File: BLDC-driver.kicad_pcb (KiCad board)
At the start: 2 copper layers, 9 parts, among them Q1 IPD50R380CE, Q2 IPD50R380CE, Q3 IPD50R380CE, Q4 IPD50R380CE, U1 NCP81151

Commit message: Schematic progress
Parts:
- added C10: 100nF, Capacitor_SMD:C_0603_1608Metric, F.Cu at (155.2, 123.5)
- added C11: 4.7uF, Capacitor_SMD:C_0603_1608Metric, F.Cu at (155.2, 126.0)
- added C12: 4.7uF, Capacitor_SMD:C_0603_1608Metric, F.Cu at (159.3, 123.5)
- added C5: 4.7uF, Capacitor_SMD:C_0603_1608Metric, F.Cu at (159.3, 126.0)
- added C6: 100nF, Capacitor_SMD:C_0603_1608Metric, F.Cu at (147.2, 123.5)
- added C7: 4.7uF, Capacitor_SMD:C_0603_1608Metric, F.Cu at (151.2, 123.5)
- added C8: 4.7uF, Capacitor_SMD:C_0603_1608Metric, F.Cu at (147.2, 126.0)
- added C9: 4.7uF, Capacitor_SMD:C_0603_1608Metric, F.Cu at (151.2, 126.0)
- added Q5: FDMS86550, Package_TO_SOT_SMD:TDSON-8-1, B.Cu at (205.4, 108.4)
- added Q6: FDMS86550, Package_TO_SOT_SMD:TDSON-8-1, B.Cu at (204.3, 101.9)
- added U2: NCP81151, Package_DFN_QFN:DFN-8-1EP_2x2mm_P0.5mm_EP0.9x1.3mm, F.Cu at (207.3, 114.1)
- added U3: NCP81151, Package_DFN_QFN:DFN-8-1EP_2x2mm_P0.5mm_EP0.9x1.3mm, F.Cu at (189.8, 113.4)
- added U4: LPC1112FHN33-101, Package_DFN_QFN:QFN-32-1EP_7x7mm_P0.65mm_EP4.7x4.7mm, F.Cu at (177.3, 121.7)
- Q1, Q2, Q3, Q4: value IPD50R380CE -> FDMS86550; footprint Package_TO_SOT_SMD:TO-252-2 -> Package_TO_SOT_SMD:TDSON-8-1; moved to B.Cu
- moved C1 34.7 mm to (196.9, 111.7), turned to 180 degrees
- moved U1 30.4 mm to (196.9, 114.0)
- moved Q2 18.3 mm to (188.3, 101.9)
- moved Q4 16.5 mm to (196.6, 101.9), turned to 0 degrees
- moved Q1 13.1 mm to (189.4, 108.4), turned to 270 degrees
- moved Q3 9.89 mm to (197.5, 108.4), turned to 270 degrees
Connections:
- Q1 pad 1: Net-(Q1-Pad1) -> /PH_C
- Q1 pad 2: +24V -> /PH_C
- Q1 pad 3: /PH_A -> /PH_C
- Q2 pad 1: Net-(Q2-Pad1) -> GND
- Q2 pad 2: /PH_A -> GND
- Q3 pad 1: Net-(Q1-Pad1) -> /PH_A
- Q3 pad 2: +24V -> /PH_A
- Q4 pad 1: Net-(Q2-Pad1) -> GND
- Q4 pad 2: /PH_A -> GND
- U1 pad 2: Net-(U1-Pad2) -> (no net)
- U1 pad 3: Net-(U1-Pad3) -> (no net)
- U1 pad 5: Net-(Q2-Pad1) -> /LG_A
- U1 pad 8: Net-(Q1-Pad1) -> /HG_A
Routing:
- net GND: track 0.00 -> 7.62 mm
- net /PH_C: track 0.00 -> 5.61 mm, vias 0 -> 16
- net /PH_B: track 0.00 -> 4.89 mm, vias 0 -> 16
- net /PH_A: track 0.00 -> 4.89 mm, vias 0 -> 16
- net Net-(C1-Pad2): track 0.00 -> 1.64 mm
- added copper zone on B.Cu, net /PH_A
- added copper zone on B.Cu, net /PH_B
- added copper zone on B.Cu, net /PH_C
- added copper zone on F.Cu, net /PH_C
- added copper zone on B.Cu, net GND
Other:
- board outline added: 55.4 x 55.6 mm

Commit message: Latest
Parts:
- added C13: 2.7nF, Capacitor_SMD:C_0603_1608Metric, F.Cu at (200.0, 105.4)
- added C14: 2.7nF, Capacitor_SMD:C_0603_1608Metric, F.Cu at (208.0, 105.2)
- added C15: 2.7nF, Capacitor_SMD:C_0603_1608Metric, F.Cu at (191.3, 104.4)
- added C16: 4.7uF, Capacitor_SMD:C_1206_3216Metric, F.Cu at (199.4, 115.8)
- added C17: 4.7uF, Capacitor_SMD:C_1206_3216Metric, F.Cu at (192.3, 115.8)
- added C18: 4.7uF, Capacitor_SMD:C_1206_3216Metric, F.Cu at (201.7, 115.8)
- added R1: 2.2, Resistor_SMD:R_0603_1608Metric, F.Cu at (197.8, 106.2)
- added R2: 2.2, Resistor_SMD:R_0603_1608Metric, F.Cu at (205.7, 106.0)
- added R3: 2.2, Resistor_SMD:R_0603_1608Metric, F.Cu at (189.1, 105.2)
- added R4: 10k, Resistor_SMD:R_0603_1608Metric, F.Cu at (183.0, 105.9)
- added TH1: 10k, Resistor_SMD:R_0603_1608Metric, F.Cu at (185.2, 107.4)
- added U5: AS5600, Package_SO:SOIC-8_3.9x4.9mm_P1.27mm, B.Cu at (195.2, 123.1)
- C11, C12, C2, C3, C7, C8: footprint Capacitor_SMD:C_0603_1608Metric -> Capacitor_SMD:C_1206_3216Metric
- U1, U2, U3: footprint Package_DFN_QFN:DFN-8-1EP_2x2mm_P0.5mm_EP0.9x1.3mm -> Package_DFN_QFN:DFN-8-1EP_2x2mm_P0.5mm_EP0.9x1.5mm
- moved C8 57.6 mm to (204.0, 115.8), turned to 270 degrees
- moved C7 55.5 mm to (206.2, 115.8), turned to 270 degrees
- moved C9 55.3 mm to (204.7, 111.6)
- moved C10 51.0 mm to (203.6, 107.1)
- moved C6 43.4 mm to (187.6, 107.4)
- moved C11 42.9 mm to (197.0, 115.8), turned to 270 degrees
- moved C12 36.1 mm to (194.6, 115.8), turned to 270 degrees
- moved C5 32.6 mm to (188.5, 111.6)
- moved C4 24.6 mm to (196.5, 111.6)
- moved U2 18.6 mm to (189.3, 109.6)
- moved C3 17.8 mm to (189.9, 115.8), turned to 270 degrees
- moved C2 17.5 mm to (187.6, 115.8), turned to 270 degrees
- moved U3 16.2 mm to (205.6, 109.6)
- moved C1 4.61 mm to (195.3, 107.4), turned to 0 degrees
- moved U1 4.47 mm to (197.5, 109.6)
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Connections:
- U1 pad 2: (no net) -> /PWM_A
- U1 pad 3: (no net) -> +5V
- U2 pad 2: (no net) -> /PWM_C
- U2 pad 3: (no net) -> +5V
- U3 pad 2: (no net) -> /PWM_B
- U3 pad 3: (no net) -> +5V
- U4 pad 1: (no net) -> Net-(U4-Pad1)
- U4 pad 10: (no net) -> Net-(U4-Pad10)
- U4 pad 11: (no net) -> Net-(U4-Pad11)
- U4 pad 12: (no net) -> Net-(U4-Pad12)
- U4 pad 13: (no net) -> Net-(U4-Pad13)
- U4 pad 14: (no net) -> Net-(U4-Pad14)
- U4 pad 15: (no net) -> Net-(U4-Pad15)
- U4 pad 16: (no net) -> Net-(U4-Pad16)
- U4 pad 17: (no net) -> /ENBL
- U4 pad 18: (no net) -> /PWM_C
- U4 pad 19: (no net) -> /PWM_A
- U4 pad 2: (no net) -> Net-(U4-Pad2)
- U4 pad 20: (no net) -> Net-(U4-Pad20)
- U4 pad 21: (no net) -> /PWM_B
- U4 pad 22: (no net) -> Net-(U4-Pad22)
- U4 pad 23: (no net) -> Net-(U4-Pad23)
- U4 pad 24: (no net) -> Net-(U4-Pad24)
- U4 pad 25: (no net) -> Net-(U4-Pad25)
- U4 pad 26: (no net) -> Net-(U4-Pad26)
- U4 pad 27: (no net) -> Net-(U4-Pad27)
- U4 pad 28: (no net) -> Net-(U4-Pad28)
- U4 pad 29: (no net) -> +3V3
- U4 pad 3: (no net) -> Net-(U4-Pad3)
- U4 pad 30: (no net) -> Net-(U4-Pad30)
- U4 pad 31: (no net) -> Net-(U4-Pad31)
- U4 pad 32: (no net) -> Net-(U4-Pad32)
- U4 pad 4: (no net) -> Net-(U4-Pad4)
- U4 pad 5: (no net) -> Net-(U4-Pad5)
- U4 pad 6: (no net) -> +3V3
- U4 pad 7: (no net) -> Net-(U4-Pad7)
- U4 pad 8: (no net) -> Net-(U4-Pad8)
- U4 pad 9: (no net) -> Net-(U4-Pad9)
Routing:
- net GND: track 7.62 -> 85.8 mm, vias 0 -> 20
- net /PWM_B: track 0.00 -> 59.7 mm, vias 0 -> 2
- net +5V: track 0.00 -> 37.2 mm
- net +24V: track 0.00 -> 30.3 mm, vias 0 -> 11
- net /PWM_A: track 0.00 -> 25.7 mm, vias 0 -> 2
- net /LG_B: track 0.00 -> 17.7 mm, vias 0 -> 1
- net /FET_TEMP: track 0.00 -> 17.5 mm
- net /LG_C: track 0.00 -> 16.5 mm, vias 0 -> 1
- net /LG_A: track 0.00 -> 15.7 mm, vias 0 -> 1
- net +3V3: track 0.00 -> 14.7 mm
- net /PWM_C: track 0.00 -> 12.6 mm
- net /PH_A: track 4.89 -> 14.8 mm, vias 16 -> 25
- net /PH_C: track 5.61 -> 14.2 mm, vias 16 -> 26
- net /PH_B: track 4.89 -> 11.7 mm, vias 16 -> 26
- net /HG_C: track 0.00 -> 2.73 mm, vias 0 -> 1
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- added copper zone on B.Cu, net +24V
- added copper zone on F.Cu, net /PH_A
- added copper zone on F.Cu, net /PH_B
- added copper zone on F.Cu, net GND
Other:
- board size 55.4 x 55.6 mm -> 55.9 x 56 mm
- board text added: "A"
- board text added: "B"
- board text added: "C"

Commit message: Latest
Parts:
- added C19: 100nF, Capacitor_SMD:C_0603_1608Metric, F.Cu at (183.8, 126.7)
- added C20: 100nF, Capacitor_SMD:C_0603_1608Metric, F.Cu at (189.9, 122.6)
- added J1: Conn_01x06, Connector_PinHeader_2.54mm:PinHeader_1x08_P2.54mm_Vertical, F.Cu at (196.3, 134.6)
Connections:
- net /ENBL renamed Net-(U4-Pad17)
- U4 pad 10: Net-(U4-Pad10) -> /SCL
- U4 pad 11: Net-(U4-Pad11) -> /SDA
- U4 pad 18: /PWM_C -> Net-(U4-Pad18)
- U4 pad 19: /PWM_A -> /SWCLK
- U4 pad 20: Net-(U4-Pad20) -> /FET_TEMP
- U4 pad 21: /PWM_B -> Net-(U4-Pad21)
- U4 pad 23: Net-(U4-Pad23) -> /PWM_C
- U4 pad 24: Net-(U4-Pad24) -> /PWM_B
- U4 pad 25: Net-(U4-Pad25) -> /SWDIO
- U4 pad 26: Net-(U4-Pad26) -> /PWM_A
- U4 pad 31: Net-(U4-Pad31) -> /RXD
- U4 pad 32: Net-(U4-Pad32) -> /TXD
- U5 pad 1: Net-(U5-Pad1) -> +3V3
- U5 pad 2: Net-(U5-Pad2) -> +3V3
- U5 pad 6: Net-(U5-Pad6) -> /SDA
- U5 pad 7: Net-(U5-Pad7) -> /SCL
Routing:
- net +3V3: track 14.7 -> 46.6 mm, vias 0 -> 4
- net +24V: track 30.3 -> 60.3 mm, vias 11 -> 47
- net /SWDIO: track 0.00 -> 18.3 mm, vias 0 -> 1
- net /SWCLK: track 0.00 -> 14.7 mm
- net /PWM_C: track 12.6 -> 23.7 mm, vias 0 -> 2
- net /PWM_A: track 25.7 -> 29.2 mm
- net GND: track 85.8 -> 88.9 mm, vias 20 -> 21
- net /FET_TEMP: track 17.5 -> 20.2 mm
- net /PWM_B: track 59.7 -> 61.5 mm
- added copper zone on F.Cu, net +24V
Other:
- board text added: "+24V"
- board text added: "GND"

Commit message: Latest
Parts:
- added C23: 10nF, Capacitor_SMD:C_0603_1608Metric, F.Cu at (212.1, 117.3)
- added C24: 1uF, Capacitor_SMD:C_0603_1608Metric, F.Cu at (214.8, 117.7)
- added C25: 1uF, Capacitor_SMD:C_0603_1608Metric, F.Cu at (208.2, 122.4)
- added C26: 1uF, Capacitor_SMD:C_0603_1608Metric, F.Cu at (202.7, 123.4)
- added C5: 100nF, Capacitor_SMD:C_0603_1608Metric, F.Cu at (172.2, 124.2)
- added C6: 100nF, Capacitor_SMD:C_0603_1608Metric, F.Cu at (179.5, 120.5)
- added D1: 30V, Diode_SMD:D_SOD-323, F.Cu at (211.2, 123.0)
- added JP1: BOOT, Jumper:SolderJumper-2_P1.3mm_Open_Pad1.0x1.5mm, F.Cu at (170.1, 127.2)
- added L1: 4.7uH, Inductor_SMD:L_Taiyo-Yuden_MD-3030, F.Cu at (212.2, 120.2)
- added NT1: Net-Tie_2, NetTie:NetTie-2_SMD_Pad0.5mm, F.Cu at (209.3, 119.5)
- added R2: 10k, Resistor_SMD:R_0603_1608Metric, F.Cu at (173.5, 131.6)
- added R3: 10k, Resistor_SMD:R_0603_1608Metric, F.Cu at (175.0, 131.6)
- added R7: 100k, Resistor_SMD:R_0603_1608Metric, F.Cu at (209.2, 113.9)
- added R8: 47k, Resistor_SMD:R_0603_1608Metric, F.Cu at (216.4, 117.7)
- added R9: 9.1k, Resistor_SMD:R_0603_1608Metric, F.Cu at (215.6, 115.4)
- added U6: MP2359, Package_TO_SOT_SMD:SOT-23-6, F.Cu at (212.1, 114.7)
- added U7: MIC5504-3.3YM5, Package_TO_SOT_SMD:SOT-23-5, F.Cu at (205.5, 122.6)
- J1: footprint Connector_PinHeader_2.54mm:PinHeader_1x08_P2.54mm_Vertical -> Connector_PinHeader_2.00mm:PinHeader_1x08_P2.00mm_Vertical
- U1: value NCP81151 -> ADP3120A
- U4: renamed from U3; value NCP81151 -> ADP3120A
- U5: renamed from U2; value NCP81151 -> ADP3120A
- moved C4 12.7 mm to (174.9, 117.7), turned to 0 degrees
- moved R1 12.1 mm to (176.5, 116.1), turned to 180 degrees
- moved NTC1 3.39 mm to (184.0, 104.2), turned to 0 degrees
- moved J1 3.11 mm to (198.9, 136.3)
- moved C13 0.16 mm to (203.5, 106.9)
- renumbered C2 to C1, C7 to C10, C8 to C11, C17 to C12, C10 to C13, C9 to C14, C11 to C15, C12 to C16, C18 to C17, C6 to C18, C5 to C19, C3 to C2, C13 to C20, C14 to C21, C15 to C22, C16 to C3, C19 to C4, C1 to C7, C4 to C8, C20 to C9, TH1 to NTC1, Q3 to Q1, Q4 to Q2, Q5 to Q3, Q6 to Q4, Q1 to Q5, Q2 to Q6, R4 to R1, R1 to R4, R2 to R5, R3 to R6, U4 to U2, U5 to U3
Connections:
- C1 pad 2: GND -> GNDPWR
- C10 pad 2: GND -> GNDPWR
- C11 pad 2: GND -> GNDPWR
- C12 pad 2: GND -> GNDPWR
- C14 pad 2: GND -> GNDPWR
- C15 pad 2: GND -> GNDPWR
- C16 pad 2: GND -> GNDPWR
- C17 pad 2: GND -> GNDPWR
- C19 pad 2: GND -> GNDPWR
- C2 pad 2: GND -> GNDPWR
- C20 pad 2: GND -> GNDPWR
- C21 pad 2: GND -> GNDPWR
- C22 pad 2: GND -> GNDPWR
- C3 pad 2: GND -> GNDPWR
- C8 pad 2: GND -> GNDPWR
- J1 pad 2: Net-(J1-Pad2) -> +5V
- J1 pad 3: /SWCLK -> /SWDIO
- J1 pad 4: /SWDIO -> /SWCLK
- J1 pad 5: /SCL -> /SDA
- J1 pad 6: /SDA -> /SCL
- NTC1 pad 1: +3V3 -> /FET_TEMP
- NTC1 pad 2: /FET_TEMP -> GNDPWR
- Q2 pad 1: GND -> GNDPWR
- Q2 pad 2: GND -> GNDPWR
- Q2 pad 3: GND -> GNDPWR
- Q4 pad 1: GND -> GNDPWR
- Q4 pad 2: GND -> GNDPWR
- Q4 pad 3: GND -> GNDPWR
- Q6 pad 1: GND -> GNDPWR
- Q6 pad 2: GND -> GNDPWR
- Q6 pad 3: GND -> GNDPWR
- R1 pad 1: /FET_TEMP -> +3V3
- R1 pad 2: GND -> /FET_TEMP
- U1 pad 6: GND -> GNDPWR
- U1 pad 9: GND -> GNDPWR
- U2 pad 20: /FET_TEMP -> Net-(U2-Pad20)
- U2 pad 3: Net-(U4-Pad3) -> /BOOT
- U2 pad 30: Net-(U4-Pad30) -> /FET_TEMP
- U4 pad 6: GND -> GNDPWR
- U4 pad 9: GND -> GNDPWR
- U5 pad 6: GND -> GNDPWR
- U5 pad 9: GND -> GNDPWR
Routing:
- net GNDPWR: track 0.00 -> 75.2 mm, vias 0 -> 59
- net +5V: track 37.2 -> 109.5 mm, vias 0 -> 4
- net GND: track 88.9 -> 17.8 mm, vias 21 -> 17
- net /SCL: track 0.00 -> 42.7 mm, vias 0 -> 1
- net /SDA: track 0.00 -> 40.0 mm, vias 0 -> 1
- net /RXD: track 0.00 -> 27.5 mm, vias 0 -> 1
- net /TXD: track 0.00 -> 25.4 mm, vias 0 -> 1
- net +3V3: track 46.6 -> 69.9 mm
- net /PWM_B: track 61.5 -> 71.4 mm
- net Net-(C23-Pad1): track 0.00 -> 7.96 mm
- net /SWDIO: track 18.3 -> 25.1 mm, vias 1 -> 2
- net /BOOT: track 0.00 -> 6.41 mm
- net Net-(R8-Pad1): track 0.00 -> 6.19 mm
- net +24V: track 60.3 -> 64.1 mm
- net /SWCLK: track 14.7 -> 17.2 mm
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- added copper zone on B.Cu, net GNDPWR
- added copper zone on F.Cu, net GNDPWR
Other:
- board text added: "+5V"
- board text added: "RXD"
- board text added: "SCL"
- board text added: "SDA"
- board text added: "SWCLK"
- board text added: "SWDIO"
- board text added: "TXD"

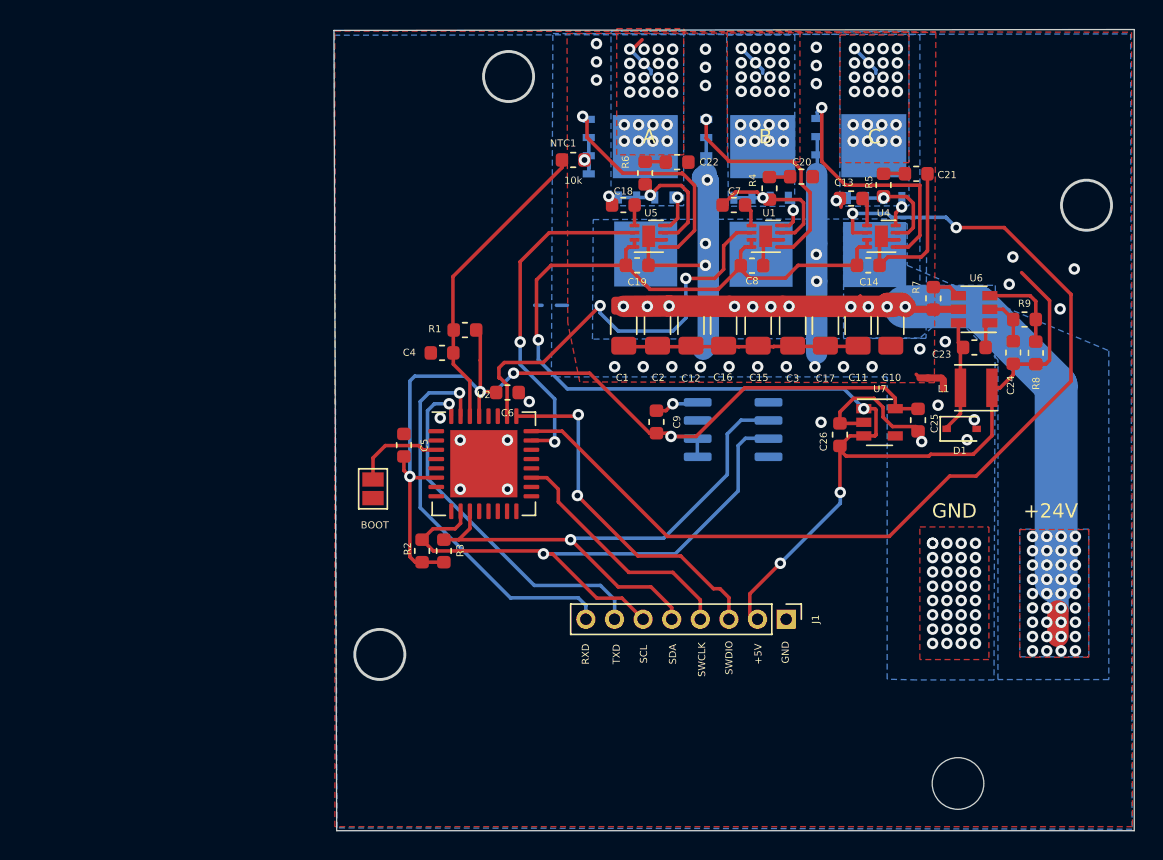
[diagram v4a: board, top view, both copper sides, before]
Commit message: Change to stm32f103c8t6
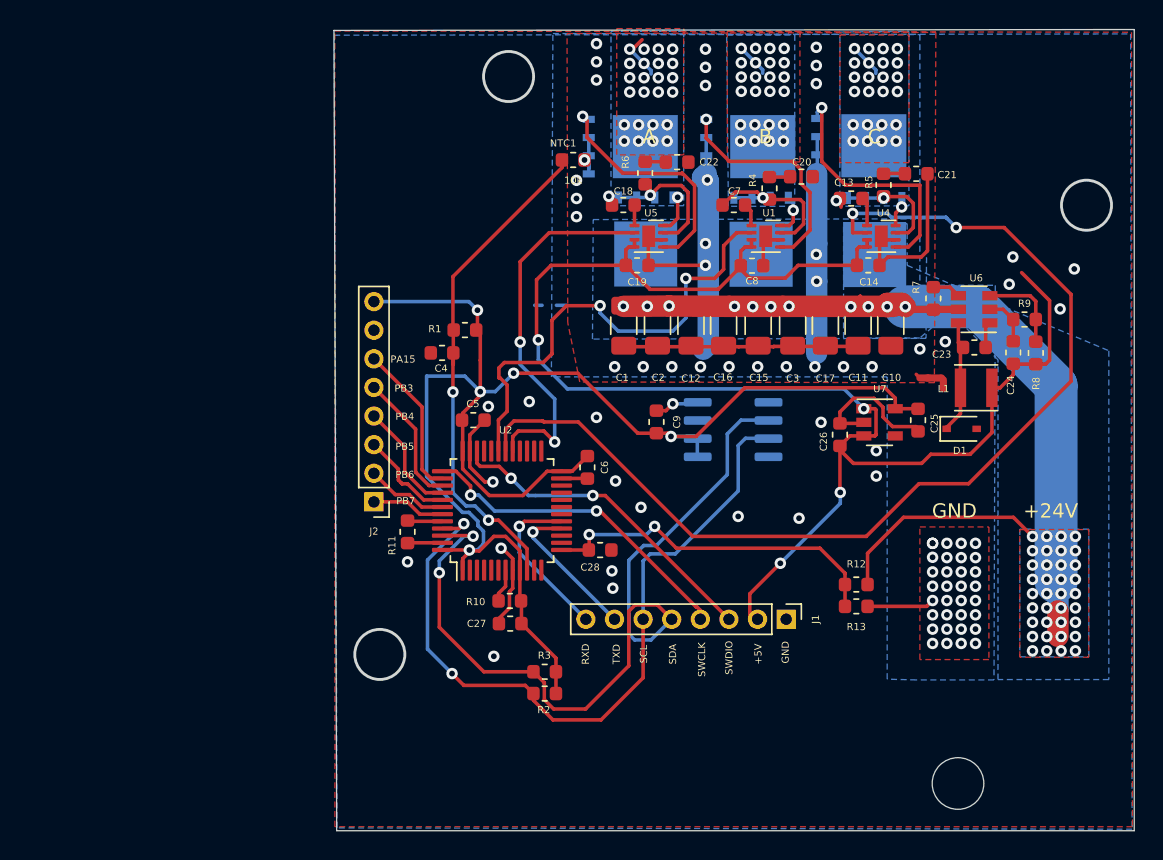
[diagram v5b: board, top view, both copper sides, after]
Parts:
- removed JP1: BOOT, Jumper:SolderJumper-2_P1.3mm_Open_Pad1.0x1.5mm
- added C27: 100nF, Capacitor_SMD:C_0603_1608Metric, F.Cu at (179.6, 136.7)
- added C28: 100nF, Capacitor_SMD:C_0603_1608Metric, F.Cu at (185.9, 131.5)
- added J2: Conn_01x06, Connector_PinHeader_2.00mm:PinHeader_1x08_P2.00mm_Vertical, F.Cu at (170.1, 128.1)
- added R10: 10k, Resistor_SMD:R_0603_1608Metric, F.Cu at (179.6, 135.1)
- added R11: 10k, Resistor_SMD:R_0603_1608Metric, F.Cu at (172.5, 130.2)
- added R12: 100k, Resistor_SMD:R_0603_1608Metric, F.Cu at (203.8, 133.9)
- added R13: 10k, Resistor_SMD:R_0603_1608Metric, F.Cu at (203.8, 135.4)
- U2: value LPC1112FHN33-101 -> STM32F103C8Tx; footprint Package_DFN_QFN:QFN-32-1EP_7x7mm_P0.65mm_EP4.7x4.7mm -> Package_QFP:LQFP-48_7x7mm_P0.5mm
- moved R2 13.1 mm to (182.1, 141.5), turned to 180 degrees
- moved R3 11.0 mm to (182.1, 140.0), turned to 180 degrees
- moved C6 7.66 mm to (185.0, 125.7), turned to 90 degrees
- moved C5 5.16 mm to (177.1, 122.4), turned to 180 degrees
- moved U2 3.51 mm to (179.1, 128.8), turned to 90 degrees
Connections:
- U2 pad 1: Net-(U2-Pad1) -> +3V3
- U2 pad 10: /SCL -> /FET_TEMP
- U2 pad 11: /SDA -> Net-(U2-Pad11)
- U2 pad 13: Net-(U2-Pad13) -> /VBUS
- U2 pad 16: Net-(U2-Pad16) -> /TXD
- U2 pad 17: Net-(U2-Pad17) -> /RXD
- U2 pad 19: /SWCLK -> Net-(U2-Pad19)
- U2 pad 23: /PWM_C -> GND
- U2 pad 24: /PWM_B -> +3V3
- U2 pad 25: /SWDIO -> Net-(U2-Pad25)
- U2 pad 26: /PWM_A -> Net-(U2-Pad26)
- U2 pad 29: +3V3 -> /PWM_C
- U2 pad 3: /BOOT -> Net-(U2-Pad3)
- U2 pad 30: /FET_TEMP -> /PWM_B
- U2 pad 31: /RXD -> /PWM_A
- U2 pad 32: /TXD -> Net-(U2-Pad32)
- U2 pad 33: GND -> Net-(U2-Pad33)
- U2 pad 6: +3V3 -> Net-(U2-Pad6)
- U2 pad 8: Net-(U2-Pad8) -> GND
- U2 pad 9: Net-(U2-Pad9) -> +3V3
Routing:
- net +3V3: track 69.9 -> 106.5 mm, vias 4 -> 5
- net /VBUS: track 0.00 -> 24.8 mm, vias 0 -> 2
- net /SDA: track 40.0 -> 59.3 mm, vias 1 -> 2
- net GND: track 17.8 -> 33.8 mm, vias 17 -> 22
- net /RXD: track 27.5 -> 11.5 mm
- net +24V: track 64.1 -> 79.4 mm
- net /TXD: track 25.4 -> 10.6 mm
- net /FET_TEMP: track 21.6 -> 35.6 mm, vias 0 -> 2
- net /PA15: track 0.00 -> 10.8 mm
- net /SCL: track 42.7 -> 52.4 mm, vias 1 -> 2
- net /PB3: track 0.00 -> 9.39 mm
- net /PB4: track 0.00 -> 8.04 mm
- net /PB5: track 0.00 -> 6.93 mm
- net /BOOT: track 6.41 -> 0.00 mm
- net /SWCLK: track 17.2 -> 23.1 mm, vias 0 -> 2
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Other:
- board text added: "PA15"
- board text added: "PB3"
- board text added: "PB4"
- board text added: "PB5"
- board text added: "PB6"
- board text added: "PB7"
